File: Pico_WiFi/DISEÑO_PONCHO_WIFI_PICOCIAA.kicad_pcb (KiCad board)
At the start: 2 copper layers, 51 x 30.5 mm, 11 parts, among them P1 MOUNT_HOLE, P2 MOUNT_HOLE, U1 ESP-12E

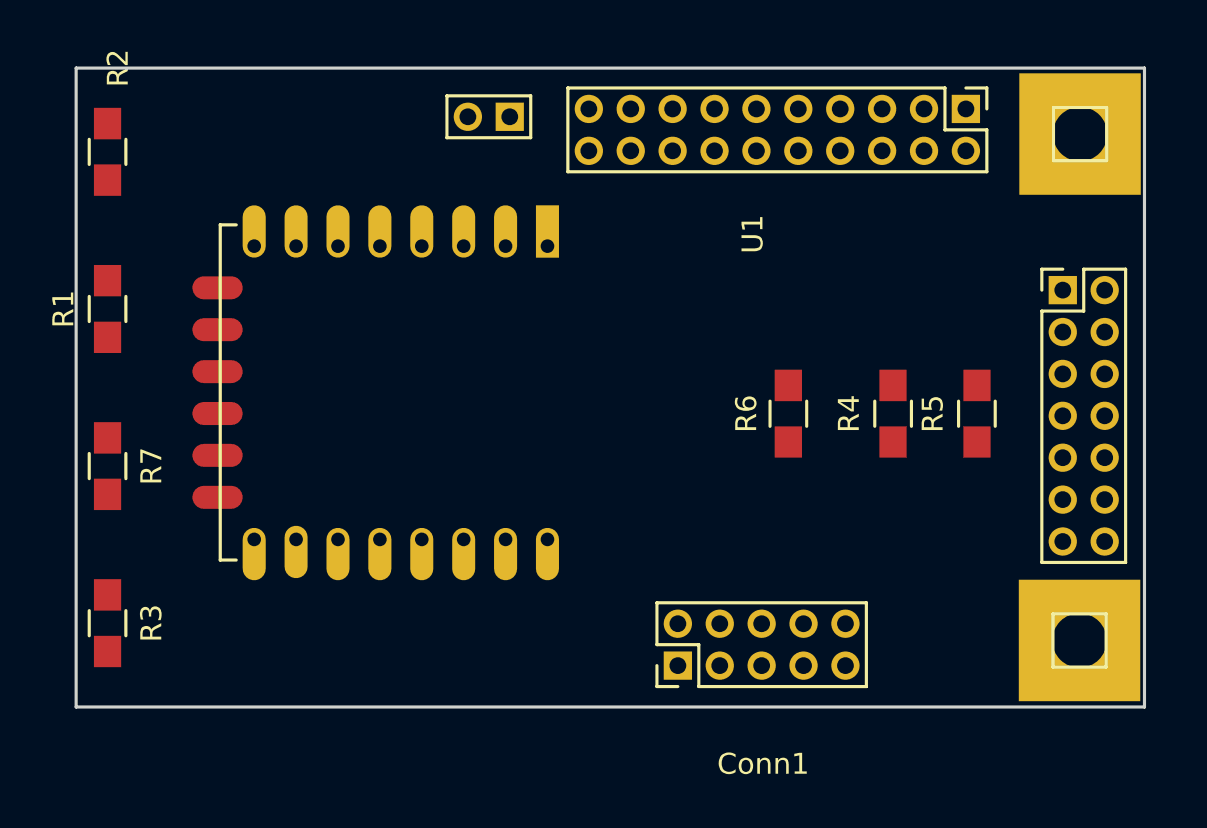
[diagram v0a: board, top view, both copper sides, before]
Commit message: Actualizo Poncho pico-wifi desde https://github.com/sergiordj/Poncho_wifi_picociaa
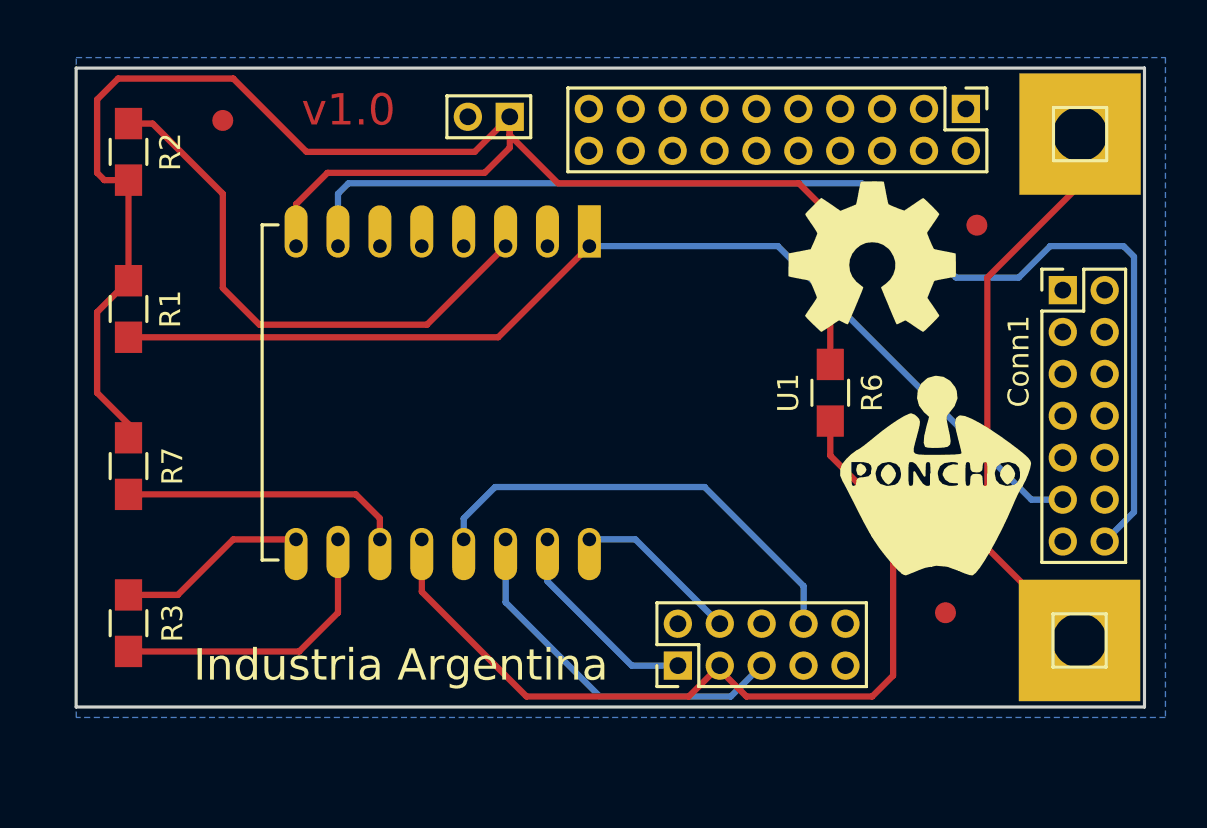
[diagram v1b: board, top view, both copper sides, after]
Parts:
- removed R4, R5: R, Resistors_SMD:R_0805_HandSoldering
- added FID1: FIDUCIAL, Poncho_wifi:Fiducial_1mm_Dia_2.54mm_Outer_CopperTop, F.Cu at (162.5, 91.5)
- added FID2: FIDUCIAL, Poncho_wifi:Fiducial_1mm_Dia_2.54mm_Outer_CopperTop, F.Cu at (161.0, 110.0)
- added FID3: FIDUCIAL, Poncho_wifi:Fiducial_1mm_Dia_2.54mm_Outer_CopperTop, F.Cu at (126.5, 86.5)
- added G***: LOGO, Poncho_wifi:Logo_Poncho, F.Cu at (160.5, 103.5)
- added G101: Logo_OSHWA, Poncho_wifi:Logo_OSHWA, F.Cu at (157.5, 93.0)
- U1: footprint pico_ciaa_ponchos:ESP-12E -> ESP-12E
- moved R6 2.24 mm to (155.5, 99.5)
- moved U1 2.00 mm to (144.0, 92.5)
- moved R1 1.00 mm to (122.0, 95.5)
- moved R2 1.00 mm to (122.0, 88.0)
- moved R3 1.00 mm to (122.0, 110.5)
- moved R7 1.00 mm to (122.0, 103.0)
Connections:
- R1 pad 1: Net-(R1-Pad1) -> Net-(Conn1-Pad11)
- U1 pad 1: Net-(R1-Pad1) -> Net-(Conn1-Pad11)
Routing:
- net +3V3: track 0.00 -> 80.6 mm
- net Net-(Conn1-Pad14): track 0.00 -> 57.6 mm
- net Net-(Conn1-Pad11): track 0.00 -> 51.4 mm
- net Net-(Conn1-Pad39): track 0.00 -> 42.2 mm
- net GND: track 0.00 -> 36.9 mm
- net Net-(R2-Pad1): track 0.00 -> 26.2 mm
- net Net-(Conn1-Pad44): track 0.00 -> 21.6 mm
- net Net-(Conn1-Pad41): track 0.00 -> 17.7 mm
- net Net-(R3-Pad2): track 0.00 -> 14.3 mm
- net Net-(R7-Pad2): track 0.00 -> 13.5 mm
- net Net-(Conn1-Pad37): track 0.00 -> 9.89 mm
- net Net-(Conn1-Pad40): track 0.00 -> 7.89 mm
- added copper zone on B.Cu, net GND
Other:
- net class Default: clearance 0.2 -> 0.3; trace_width 0.25 -> 0.3; via_dia 0.6 -> 1.27; via_drill 0.4 -> 0.7
- rule trace_clearance: 0.2 -> 0.3
- rule trace_min: 0.2 -> 0.3
- rule via_min_drill: 0.3 -> 0.7
- rule via_min_size: 0.4 -> 1.27
- board text added: "Capas de cobre: 2"
- board text added: "Espesor de placa: 1.4mm Espesor de cobre: 1Oz Soporte FR4"
- board text added: "Estándar de fabricación: Mayer 12 mils Según documento encontrado en: CONSIDERACIONES_INICIALES/FABRICANTES\ DE\ PCB/estandares.pdf"
- board text added: "Industria Argentina"
- board text added: "Poncho wifi PicoCIAA"
- board text added: "Sergio De Jesús"
- board text added: "StackUp"
- board text added: "v1.0"
